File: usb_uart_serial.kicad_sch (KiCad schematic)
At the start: 12 parts, among them Q401 MMDT3904, U301 CP2102N-Axx-xQFN28

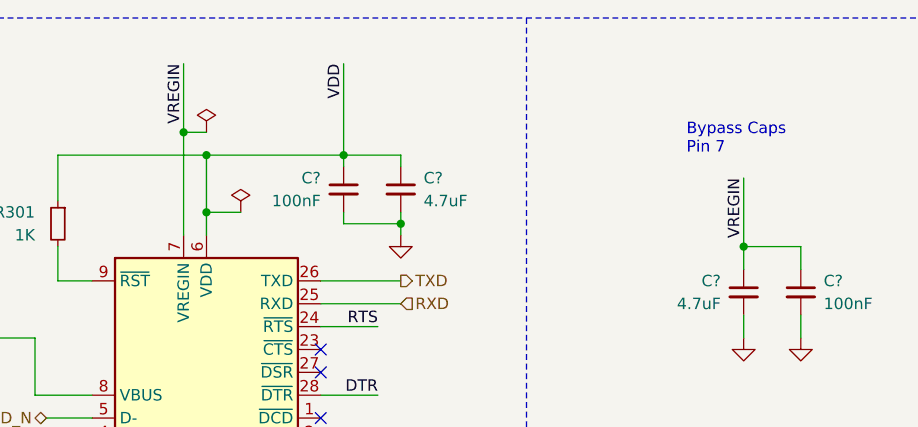
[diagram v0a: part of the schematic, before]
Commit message: refactor to accept 12V power
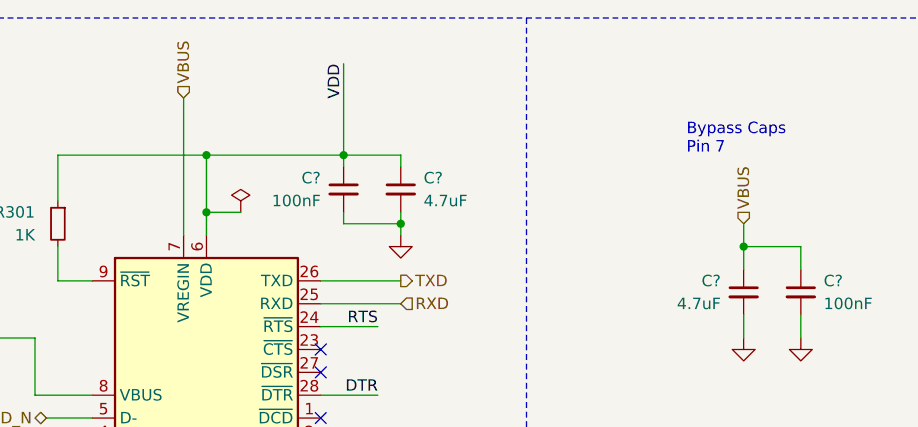
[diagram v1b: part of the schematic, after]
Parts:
- U301: LCSC (none) -> C964632; Mouser (none) -> 634-CP2102NA02GQFN28
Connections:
- net VREGIN is gone; now on net VBUS: C?.1, C?.1, U301.7 (VREGIN)
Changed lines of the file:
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@@
   (junction (at 116.84 102.87) (diameter 0) (color 0 0 0 0)
-  )
-  (junction (at 63.5 34.29) (diameter 0) (color 0 0 0 0)
   )
   (junction (at 125.73 46.99) (diameter 0) (color 0 0 0 0)
@@
     (stroke (width 0) (type default))
   )
-  (wire (pts (xy 63.5 34.29) (xy 66.04 34.29))
-    (stroke (width 0) (type default))
-  )
-  (wire (pts (xy 125.73 39.37) (xy 125.73 46.99))
+  (wire (pts (xy 125.73 44.45) (xy 125.73 46.99))
     (stroke (width 0) (type default))
   )
@@
     (stroke (width 0) (type default))
   )
-  (wire (pts (xy 63.5 26.67) (xy 63.5 34.29))
-    (stroke (width 0) (type default))
-  )
   (wire (pts (xy 114.3 85.09) (xy 119.38 85.09))
     (stroke (width 0) (type default))
@@
     (stroke (width 0) (type default))
   )
-  (wire (pts (xy 63.5 34.29) (xy 63.5 45.72))
+  (wire (pts (xy 63.5 30.48) (xy 63.5 45.72))
     (stroke (width 0) (type default))
   )
@@
     (effects (font (size 1.27 1.27)) (justify left bottom))
   )
-  (label "VREGIN" (at 125.73 39.37 270) (fields_autoplaced)
-    (effects (font (size 1.27 1.27)) (justify right bottom))
-  )
   (label "RTS" (at 85.09 55.88 180) (fields_autoplaced)
     (effects (font (size 1.27 1.27)) (justify right bottom))
@@
     (effects (font (size 1.27 1.27)) (justify left bottom))
   )
-  (label "VREGIN" (at 63.5 26.67 270) (fields_autoplaced)
-    (effects (font (size 1.27 1.27)) (justify right bottom))
-  )
   (hierarchical_label "IO0" (shape output) (at 143.51 111.76 0) (fields_autoplaced)
+    (effects (font (size 1.27 1.27)) (justify left))
+  )
+  (hierarchical_label "VBUS" (shape input) (at 63.5 30.48 90) (fields_autoplaced)
     (effects (font (size 1.27 1.27)) (justify left))
   )
@@
   (hierarchical_label "D_P" (shape bidirectional) (at 48.26 68.58 180) (fields_autoplaced)
     (effects (font (size 1.27 1.27)) (justify right))
+  )
+  (hierarchical_label "VBUS" (shape input) (at 125.73 44.45 90) (fields_autoplaced)
+    (effects (font (size 1.27 1.27)) (justify left))
   )
   (hierarchical_label "D_N" (shape bidirectional) (at 48.26 66.04 180) (fields_autoplaced)
@@
     )
     (property "Datasheet" "https://www.silabs.com/documents/public/data-sheets/cp2102n-datasheet.pdf" (at 67.31 97.79 0)
+      (effects (font (size 1.27 1.27)) hide)
+    )
+    (property "LCSC" "C964632" (at 66.04 78.74 0)
+      (effects (font (size 1.27 1.27)) hide)
+    )
+    (property "Mouser" "634-CP2102NA02GQFN28" (at 66.04 78.74 0)
       (effects (font (size 1.27 1.27)) hide)
     )
@@
         )
       )
-    )
-  )
-  (symbol (lib_id "power:PWR_FLAG") (at 66.04 34.29 0) (unit 1)
-    (in_bom yes) (on_board yes) (dnp no) (fields_autoplaced)
-    (property "Reference" "#FLG0302" (at 66.04 32.385 0)
-      (effects (font (size 1.27 1.27)) hide)
-    )
-    (property "Value" "PWR_FLAG" (at 66.04 29.21 0)
-      (effects (font (size 1.27 1.27)) hide)
-    )
-    (property "Footprint" "" (at 66.04 34.29 0)
-      (effects (font (size 1.27 1.27)) hide)
-    )
-    (property "Datasheet" "~" (at 66.04 34.29 0)
-      (effects (font (size 1.27 1.27)) hide)
-    )
-    (pin "1")
-    (instances
-      (project "mini-project-1-arduino-uno-clone"
-        (path "/381cc05b-6777-4559-a85b-686b87a5591b/4ec7cffb-62ae-4955-a68d-63ae97a4022c"
-          (reference "#FLG0302") (unit 1)
-        )
-      )
-      (project "wled-esp32-control-board"
-        (path "/39949f26-7b4e-4f4c-975a-4ef261468b2a/7ba064c5-609e-4a93-bc47-f12eb1cc9f1a"
-          (reference "#FLG0401") (unit 1)
-        )
-      )
